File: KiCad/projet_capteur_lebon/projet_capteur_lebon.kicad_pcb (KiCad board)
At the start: 2 copper layers, 68.6 x 53.3 mm, 18 parts, among them J1 Power, J2 Digital/PWM, J3 Analog, J4 Digital/PWM

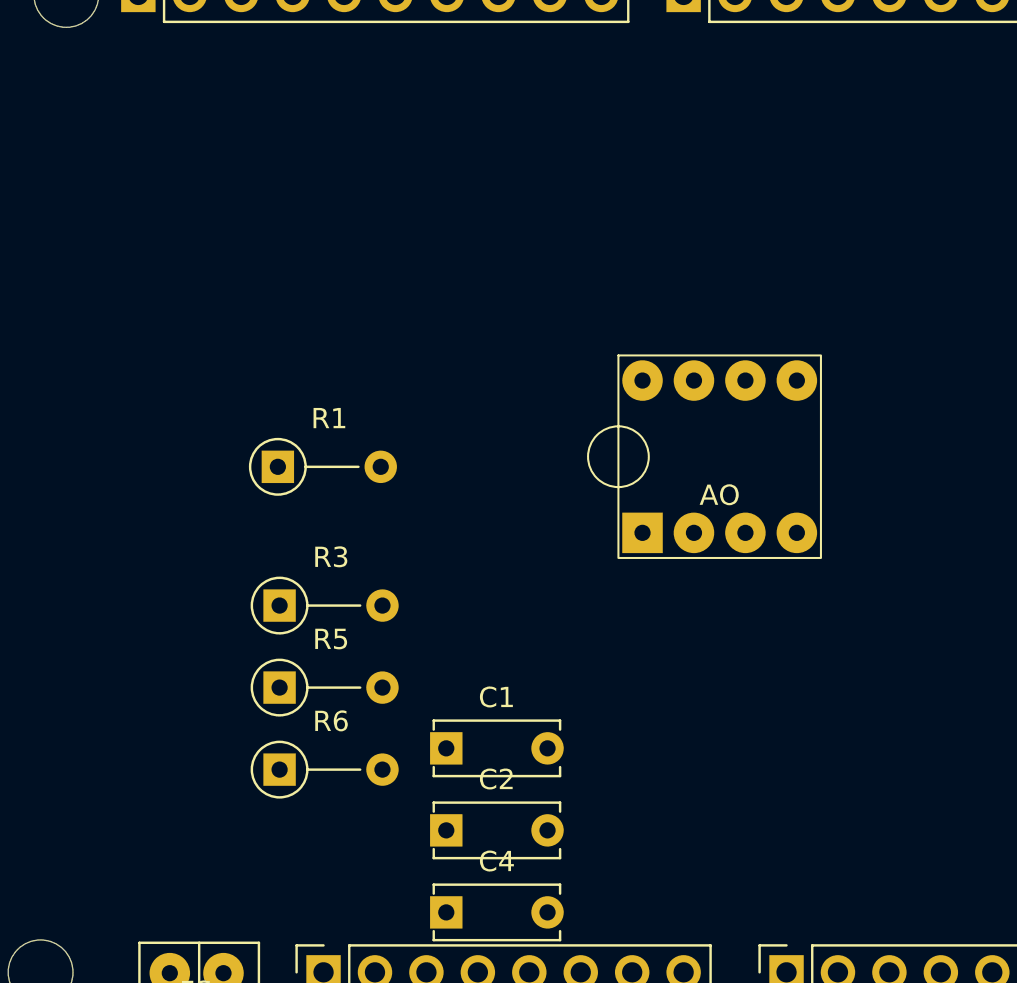
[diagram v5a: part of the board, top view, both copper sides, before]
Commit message: mep bluetooth et fin ampli
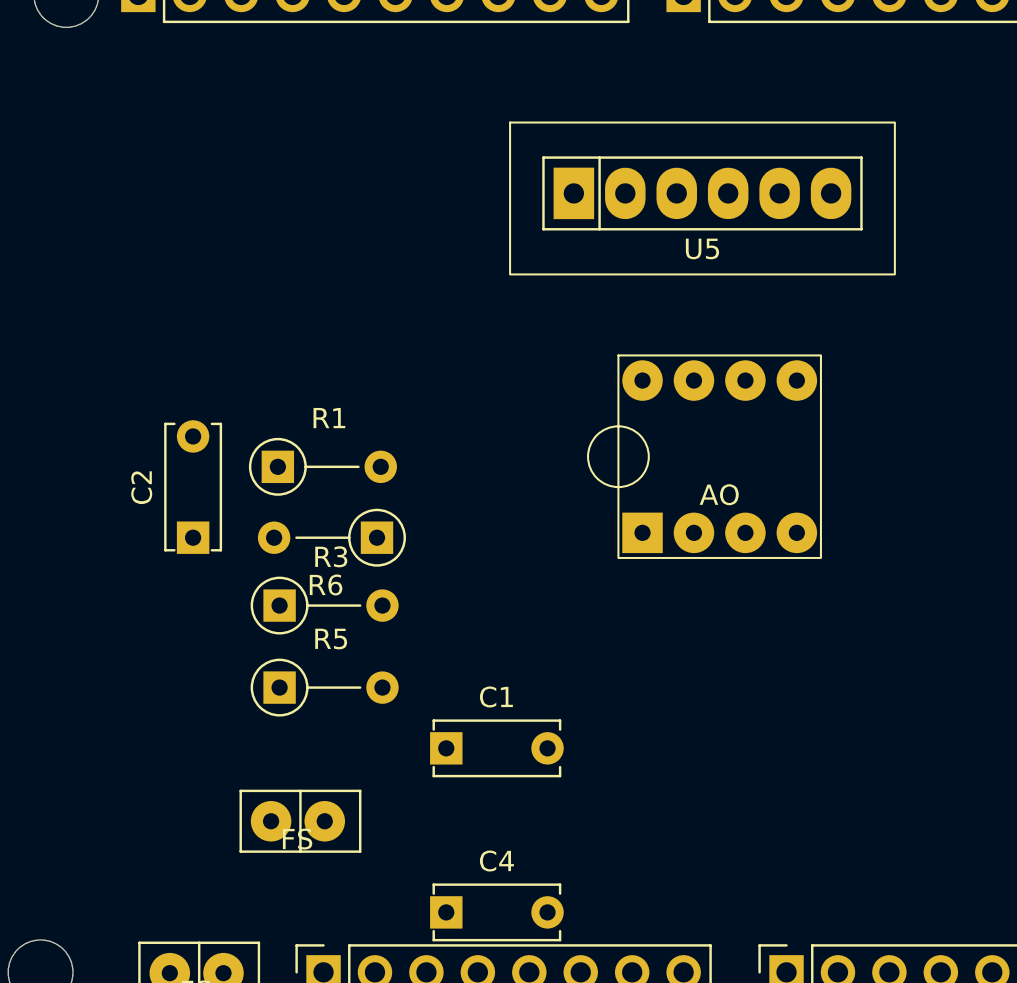
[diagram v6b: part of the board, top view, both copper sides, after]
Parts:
- added U3: ~, librairie_empreintes:SIP-2, F.Cu at (126.8, 90.8)
- added U5: ~, librairie_empreintes:BLUETOOTH, F.Cu at (146.7, 59.0)
- moved C2 19.1 mm to (121.5, 76.0), turned to 90 degrees
- moved R6 12.4 mm to (130.6, 76.0), turned to 180 degrees

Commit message: encodeur rot + verifs
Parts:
- removed U1: ~, librairie_empreintes:SIP-4
- removed U5: ~, librairie_empreintes:BLUETOOTH
- added R2: 47k, librairie_empreintes:R_Axial_DIN0207_L6.3mm_D2.5mm_P5.08mm_Vertical, F.Cu at (116.4, 63.0)
- added REF**: BLUETOOTH, librairie_empreintes:BLUETOOTH, F.Cu at (151.0, 60.5)
- added REF**: SIP-4, librairie_empreintes:SIP-4, F.Cu at (166.5, 75.7)
- U2: footprint librairie_empreintes:SIP-2 -> librairie_empreintes:ENCODEUR ROT
- moved U2 24.1 mm to (110.4, 77.0)

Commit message: Etiquette
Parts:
- removed REF**: BLUETOOTH, librairie_empreintes:BLUETOOTH
- removed REF**: SIP-4, librairie_empreintes:SIP-4
- added C3: c, librairie_empreintes:C_Disc_D6.0mm_W2.5mm_P5.00mm, F.Cu at (102.0, 74.0)
- added U1: ~, librairie_empreintes:SIP-4, F.Cu at (165.5, 77.7)
- added U5: ~, librairie_empreintes:BLUETOOTH, F.Cu at (155.7, 55.0)
- moved U2 3.19 mm to (111.5, 80.0)
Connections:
- U2 pad 1: unconnected-(U2-CLK-Pad1) -> EROT 1
- U2 pad 2: unconnected-(U2-DT-Pad2) -> EROT 2
- U2 pad 3: unconnected-(U2-SW-Pad3) -> EROT 3
- U2 pad 4: unconnected-(U2-VCC-Pad4) -> 5V
- U3 pad 1: unconnected-(U3-EN-Pad1) -> BT 1
- U3 pad 2: unconnected-(U3-VCC-Pad2) -> 5V
